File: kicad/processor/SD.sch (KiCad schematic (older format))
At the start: 5 parts, among them M501 MICROSD, Q501 DMG3415U

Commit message: Restructure directories - separate projects for each board,
separate directory for analysis, datasheets
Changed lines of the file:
@@
 EESchema Schematic File Version 2
-LIBS:paddle-rescue
-LIBS:paddle
-LIBS:adafruit
 LIBS:power
 LIBS:device
@@
 LIBS:linear
 LIBS:regul
-LIBS:74xx
-LIBS:cmos4000
-LIBS:adc-dac
-LIBS:memory
-LIBS:xilinx
-LIBS:microcontrollers
-LIBS:dsp
-LIBS:microchip
-LIBS:analog_switches
-LIBS:motorola
-LIBS:texas
-LIBS:intel
-LIBS:audio
-LIBS:interface
-LIBS:digital-audio
-LIBS:philips
-LIBS:display
-LIBS:cypress
-LIBS:siliconi
-LIBS:opto
-LIBS:atmel
-LIBS:contrib
-LIBS:valves
-LIBS:diode
-LIBS:switches
-LIBS:paddle-cache
+LIBS:paddle
 EELAYER 25 0
 EELAYER END
 $Descr A4 11693 8268
 encoding utf-8
-Sheet 4 13
+Sheet 4 5
 Title ""
 Date ""
@@
 	5300 3800 5300 3900
 Wire Wire Line
-	5100 3800 5300 3800
-Wire Wire Line
-	5300 3800 5750 3800
-Wire Wire Line
-	5750 3800 6100 3800
+	5100 3800 6100 3800
 Connection ~ 6000 4100
 Wire Wire Line
@@
 	6100 4100 6000 4100
 Wire Wire Line
-	6000 3900 6000 4100
-Wire Wire Line
-	6000 4100 6000 4200
-Wire Wire Line
-	6000 4200 6000 4300
+	6000 3900 6000 4300
 Wire Wire Line
 	6000 4200 6100 4200
@@
 	4650 3150 4650 3200
 Wire Wire Line
-	4450 3600 4650 3600
-Wire Wire Line
-	4650 3600 4800 3600
+	4450 3600 4800 3600
 Connection ~ 4650 3600
 Text HLabel 4450 3600 0    60   Input ~ 0

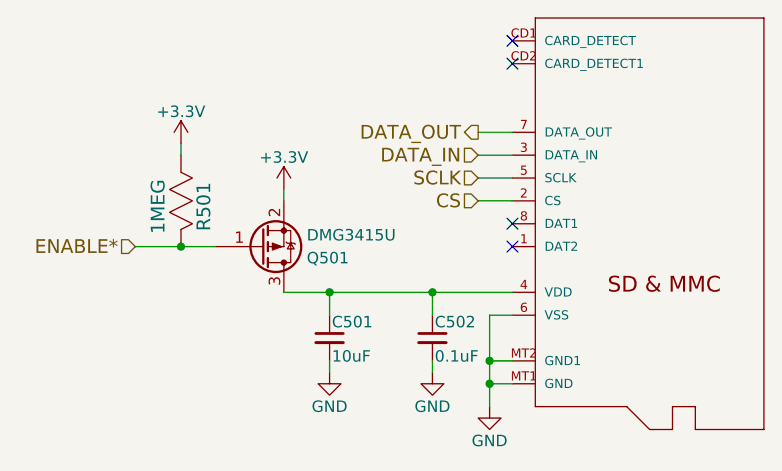
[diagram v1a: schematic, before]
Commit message: Finish split projects, fix ERC, import outline to processor board
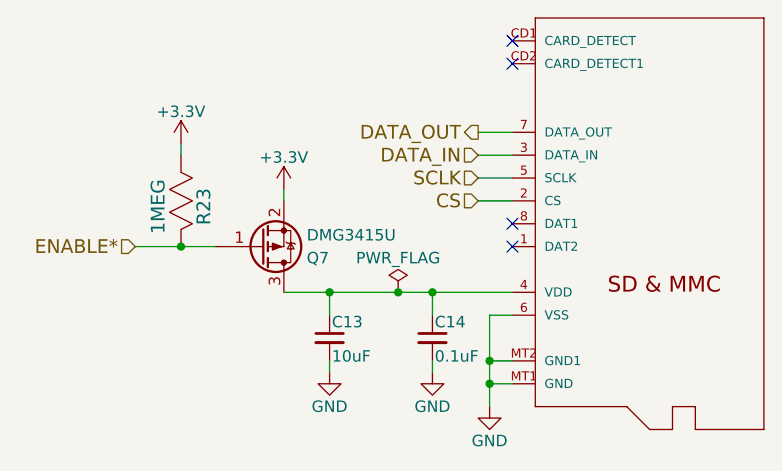
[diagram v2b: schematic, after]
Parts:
- renumbered C501 to C13, C502 to C14, M501 to M1, Q501 to Q7, R501 to R23
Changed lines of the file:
@@
 LIBS:regul
 LIBS:paddle
+LIBS:processor-cache
 EELAYER 25 0
 EELAYER END
@@
 $EndDescr
 $Comp
-L MICROSD M501
+L MICROSD M1
 U 1 1 59CAB903
 P 6800 3400
-F 0 "M501" H 6800 3400 45  0001 C CNN
+F 0 "M1" H 6800 3400 45  0001 C CNN
 F 1 "MICROSD" H 6800 3400 45  0001 C CNN
 F 2 "adafruit:MICROSD" H 6830 3550 20  0001 C CNN
@@
 $EndComp
 $Comp
-L GND #PWR405
+L GND #PWR058
 U 1 1 59CAB909
 P 6000 4300
-F 0 "#PWR405" H 6000 4050 50  0001 C CNN
+F 0 "#PWR058" H 6000 4050 50  0001 C CNN
 F 1 "GND" H 6000 4150 50  0000 C CNN
 F 2 "" H 6000 4300 50  0001 C CNN
@@
 $EndComp
 $Comp
-L +3.3V #PWR402
+L +3.3V #PWR059
 U 1 1 59CAB90F
 P 5100 3350
-F 0 "#PWR402" H 5100 3200 50  0001 C CNN
+F 0 "#PWR059" H 5100 3200 50  0001 C CNN
 F 1 "+3.3V" H 5100 3490 50  0000 C CNN
 F 2 "" H 5100 3350 50  0001 C CNN
@@
 NoConn ~ 6100 3600
 $Comp
-L C_Small C502
+L C_Small C14
 U 1 1 59CAB919
 P 5750 4000
-F 0 "C502" H 5760 4070 50  0000 L CNN
+F 0 "C14" H 5760 4070 50  0000 L CNN
 F 1 "0.1uF" H 5760 3920 50  0000 L CNN
 F 2 "paddle:SMD_0805" H 5750 4000 50  0001 C CNN
@@
 $EndComp
 $Comp
-L GND #PWR404
+L GND #PWR060
 U 1 1 59CAB920
 P 5750 4150
-F 0 "#PWR404" H 5750 3900 50  0001 C CNN
+F 0 "#PWR060" H 5750 3900 50  0001 C CNN
 F 1 "GND" H 5750 4000 50  0000 C CNN
 F 2 "" H 5750 4150 50  0001 C CNN
@@
 $EndComp
 $Comp
-L C_Small C501
+L C_Small C13
 U 1 1 59CAB926
 P 5300 4000
-F 0 "C501" H 5310 4070 50  0000 L CNN
+F 0 "C13" H 5310 4070 50  0000 L CNN
 F 1 "10uF" H 5310 3920 50  0000 L CNN
 F 2 "paddle:SMD_1206" H 5300 4000 50  0001 C CNN
@@
 $EndComp
 $Comp
-L GND #PWR403
+L GND #PWR061
 U 1 1 59CAB92D
 P 5300 4150
-F 0 "#PWR403" H 5300 3900 50  0001 C CNN
+F 0 "#PWR061" H 5300 3900 50  0001 C CNN
 F 1 "GND" H 5300 4000 50  0000 C CNN
 F 2 "" H 5300 4150 50  0001 C CNN
@@
 	5100 3350 5100 3400
 $Comp
-L Q_PMOS_GSD Q501
+L Q_PMOS_GSD Q7
 U 1 1 59CAC052
 P 5000 3600
-F 0 "Q501" H 5200 3650 50  0000 L CNN
+F 0 "Q7" H 5200 3650 50  0000 L CNN
 F 1 "DMG3415U" H 5200 3550 50  0000 L CNN
 F 2 "paddle:SOT-23" H 5200 3700 50  0001 C CNN
@@
 $EndComp
 $Comp
-L R_US R501
+L R_US R23
 U 1 1 59CAC2F3
 P 4650 3400
-F 0 "R501" H 4675 3500 60  0000 C CNN
+F 0 "R23" H 4675 3500 60  0000 C CNN
 F 1 "1MEG" H 4675 3300 60  0000 C CNN
 F 2 "paddle:SMD_0805" H 4650 3050 60  0001 C CNN
@@
 $EndComp
 $Comp
-L +3.3V #PWR401
+L +3.3V #PWR062
 U 1 1 59CAC2FA
 P 4650 3150
-F 0 "#PWR401" H 4650 3000 50  0001 C CNN
+F 0 "#PWR062" H 4650 3000 50  0001 C CNN
 F 1 "+3.3V" H 4650 3290 50  0000 C CNN
 F 2 "" H 4650 3150 50  0001 C CNN
@@
 Wire Wire Line
 	6100 3400 5950 3400
+$Comp
+L PWR_FLAG #FLG063
+U 1 1 59FFCAED
+P 5600 3800
+F 0 "#FLG063" H 5600 3875 50  0001 C CNN
+F 1 "PWR_FLAG" H 5600 3950 50  0000 C CNN
+F 2 "" H 5600 3800 50  0001 C CNN
+F 3 "" H 5600 3800 50  0001 C CNN
+	1    5600 3800
+	1    0    0    -1
+$EndComp
+Connection ~ 5600 3800
 $EndSCHEMATC

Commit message: Logic board standalone about done, changed to 0603 resistors and 0805 caps
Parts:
- C13: footprint paddle:SMD_1206 -> paddle:SMD_0805
- R23: footprint paddle:SMD_0805 -> paddle:R_0603
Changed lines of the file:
@@
 F 0 "C13" H 5310 4070 50  0000 L CNN
 F 1 "10uF" H 5310 3920 50  0000 L CNN
-F 2 "paddle:SMD_1206" H 5300 4000 50  0001 C CNN
+F 2 "paddle:SMD_0805" H 5300 4000 50  0001 C CNN
 F 3 "" H 5300 4000 50  0001 C CNN
 	1    5300 4000
@@
 F 0 "R23" H 4675 3500 60  0000 C CNN
 F 1 "1MEG" H 4675 3300 60  0000 C CNN
-F 2 "paddle:SMD_0805" H 4650 3050 60  0001 C CNN
+F 2 "paddle:R_0603" H 4650 3050 60  0001 C CNN
 F 3 "" H 4675 3500 60  0000 C CNN
 	1    4650 3400

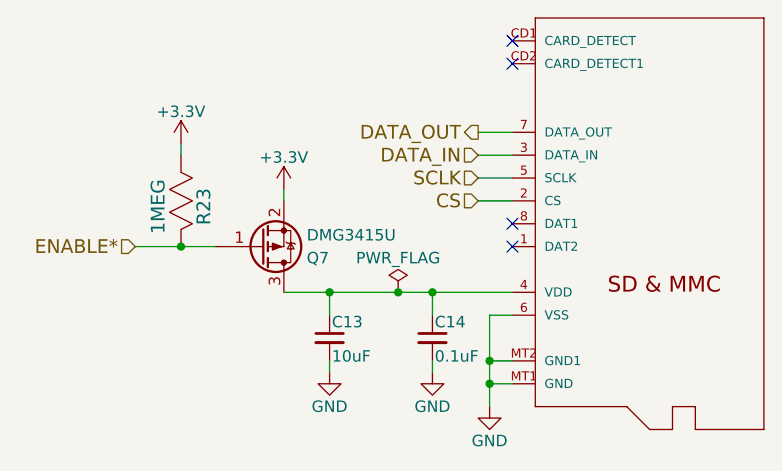
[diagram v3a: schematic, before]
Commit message: First cut layout power supply, fix netclasses, footprint for connector
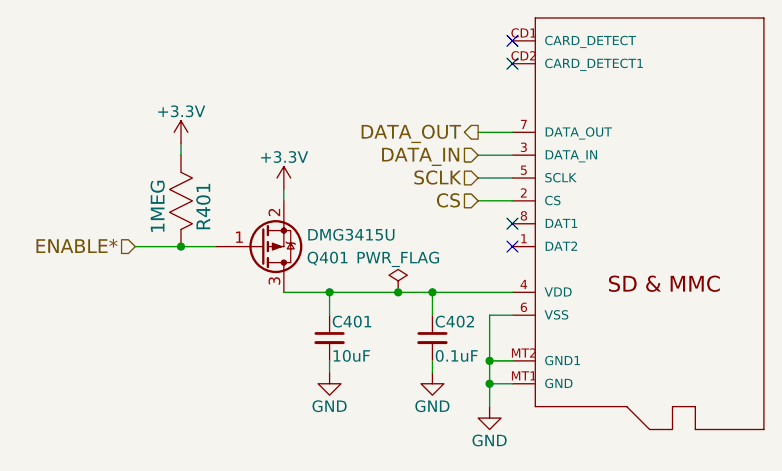
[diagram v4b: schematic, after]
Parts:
- renumbered C13 to C401, C14 to C402, M1 to M401, Q7 to Q401, R23 to R401
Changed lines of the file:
@@
 $EndDescr
 $Comp
-L MICROSD M1
+L MICROSD M401
 U 1 1 59CAB903
 P 6800 3400
-F 0 "M1" H 6800 3400 45  0001 C CNN
+F 0 "M401" H 6800 3400 45  0001 C CNN
 F 1 "MICROSD" H 6800 3400 45  0001 C CNN
 F 2 "adafruit:MICROSD" H 6830 3550 20  0001 C CNN
@@
 NoConn ~ 6100 3600
 $Comp
-L C_Small C14
+L C_Small C402
 U 1 1 59CAB919
 P 5750 4000
-F 0 "C14" H 5760 4070 50  0000 L CNN
+F 0 "C402" H 5760 4070 50  0000 L CNN
 F 1 "0.1uF" H 5760 3920 50  0000 L CNN
 F 2 "paddle:SMD_0805" H 5750 4000 50  0001 C CNN
@@
 $EndComp
 $Comp
-L C_Small C13
+L C_Small C401
 U 1 1 59CAB926
 P 5300 4000
-F 0 "C13" H 5310 4070 50  0000 L CNN
+F 0 "C401" H 5310 4070 50  0000 L CNN
 F 1 "10uF" H 5310 3920 50  0000 L CNN
 F 2 "paddle:SMD_0805" H 5300 4000 50  0001 C CNN
@@
 	5100 3350 5100 3400
 $Comp
-L Q_PMOS_GSD Q7
+L Q_PMOS_GSD Q401
 U 1 1 59CAC052
 P 5000 3600
-F 0 "Q7" H 5200 3650 50  0000 L CNN
+F 0 "Q401" H 5200 3650 50  0000 L CNN
 F 1 "DMG3415U" H 5200 3550 50  0000 L CNN
 F 2 "paddle:SOT-23" H 5200 3700 50  0001 C CNN
@@
 $EndComp
 $Comp
-L R_US R23
+L R_US R401
 U 1 1 59CAC2F3
 P 4650 3400
-F 0 "R23" H 4675 3500 60  0000 C CNN
+F 0 "R401" H 4675 3500 60  0000 C CNN
 F 1 "1MEG" H 4675 3300 60  0000 C CNN
 F 2 "paddle:R_0603" H 4650 3050 60  0001 C CNN
